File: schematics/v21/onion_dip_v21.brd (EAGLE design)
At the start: 41 x 50 mm, 36 parts, among them IC2 DS2432P

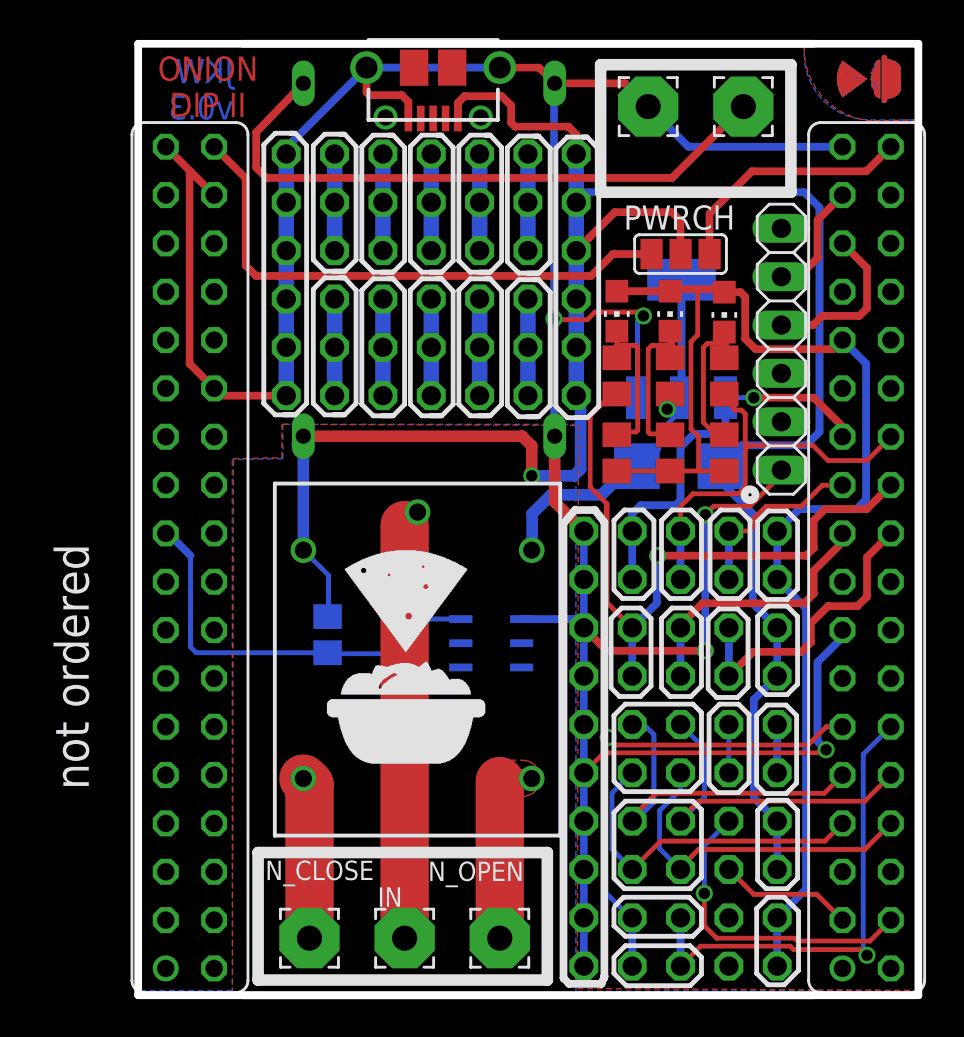
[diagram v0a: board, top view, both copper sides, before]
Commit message: added version 2.1 with corner cut and silk screen improvment
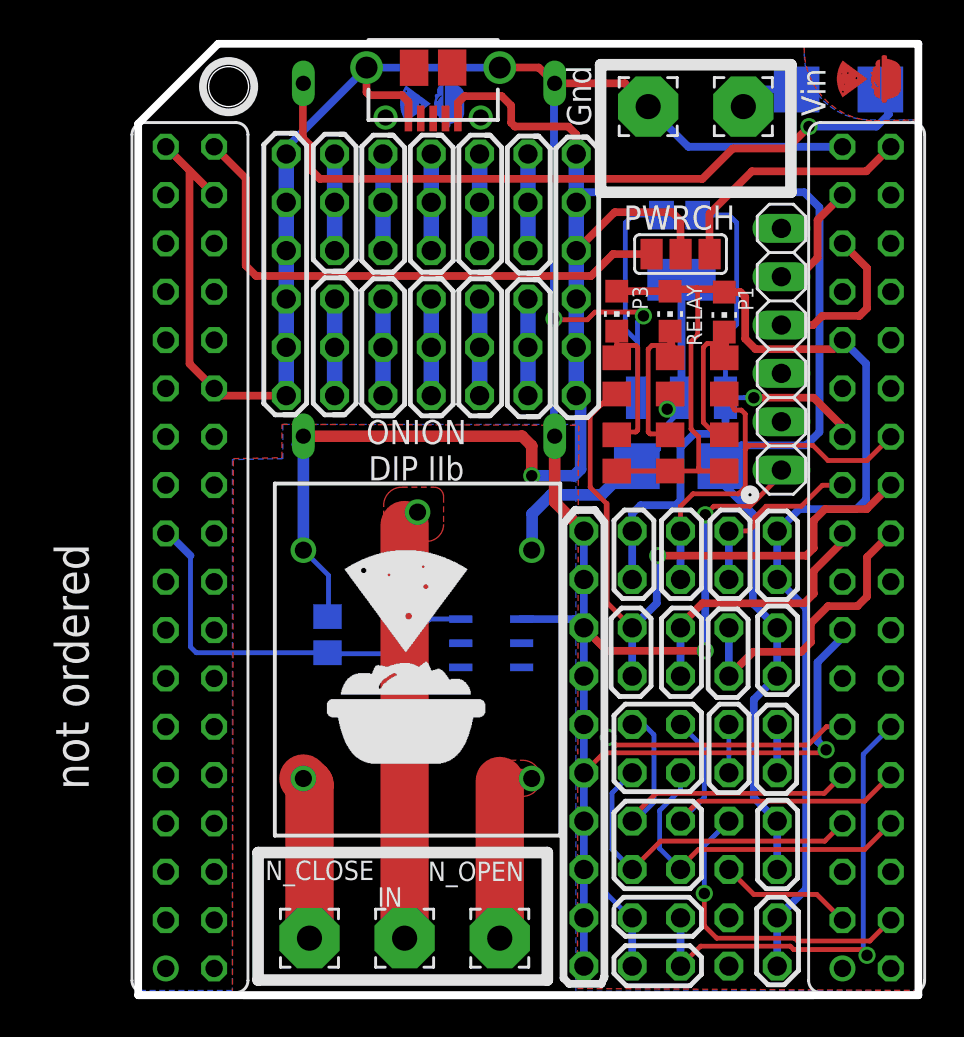
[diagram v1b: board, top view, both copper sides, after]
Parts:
- added D1: (no value), diode:SMB
- added R8: 10k, rcl:R0805
- moved U$6 23.0 mm to (15.4, 46.9)
- renumbered LED1 to P3, LED2 to P1, LED5 to RELAY
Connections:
- new net N$1: D1.C, U$9.VIN
- net GND: now also R8.2
- net P0: now also R8.1
- net VIN: now also D1.A; no longer U$9.VIN
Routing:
- net N$1: track 0.00 -> 38.1 mm, vias 0 -> 1
- net VIN: track 33.2 -> 3.17 mm
- net P0: track 20.8 -> 32.5 mm
- net GND: track 169.8 -> 178.4 mm
- added copper zone on layer 1, net RIN
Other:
- outline, holes or cut-outs redrawn
- board text added: "<--"
- board text added: "CHIP bat connector"
- board text added: "CHIP powered close right"
- board text added: "Gnd"
- board text added: "Input 5V Close left"
- board text added: "JKW v0.32"
- board text added: "ONION DIP IIb"
- board text added: "Orientation:"
- board text added: "Vin"
- board text removed: "CHIP powered -> 1&2"
- board text removed: "Input 5V: Close 3&2"
- board text removed: "JKW v0.3"
- board text removed: "ONION DIP II"
